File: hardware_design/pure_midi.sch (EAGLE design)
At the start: 60 parts, among them IC1 74HC165D, IC2 VOLTAGE_REG_POS05DT, Q1 20MHz, T1 MMBT3904, T2 MMBT3904, T3 MMBT3904, T4 MMBT3904, U1 ANALOG_DEVICES_INC_AD5754AREZ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, U2 TEXAS_INSTRUMENTS_LM4040C25ID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, U3 ATMEGA328P_TQFP, X1 OG-MIDI_MAB5SHCUI-SD-50BV

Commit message: Use different one-hot to binary encoder
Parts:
- removed IC1: 74HC165D, 74xx-eu:74HC165D
- added IC3: 74HC148D, 74xx-eu:74HC148D
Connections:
- removed net N$17: IC1A.B, R24.2, U$12.2
- removed net N$18: IC1A.C, R23.2, U$12.3
- removed net N$19: IC1A.D, R22.2, U$12.4
- removed net N$21: IC1A.E, R21.2, U$12.5
- removed net N$22: IC1A.F, R20.2, U$12.6
- removed net N$23: IC1A.G, R19.2, U$12.7
- removed net N$24: IC1A.H, R18.2, U$12.8
- removed net ROTARY_CLK: IC1A.CLK, U3.PD4(XCK/T0)
- removed net ROTARY_DAT: IC1A.QH, U3.PD2(INT0)
- removed net ROTARY_LD: IC1A.SH/!LD, U3.PD3(INT1)
- new net N$26: IC3A.1, R19.1, U$12.2
- new net N$27: IC3A.2, R20.1, U$12.3
- new net N$28: IC3A.3, R21.1, U$12.4
- new net N$29: IC3A.4, R22.1, U$12.5
- new net N$30: IC3A.5, R23.1, U$12.6
- new net N$31: IC3A.6, R24.1, U$12.7
- new net N$32: IC3A.7, R25.1, U$12.8
- new net ROTARY_D0: IC3A.A0, U3.PD2(INT0)
- new net ROTARY_D1: IC3A.A1, U3.PD3(INT1)
- new net ROTARY_D2: IC3A.A2, U3.PD4(XCK/T0)
- net +5V: now also IC3P.VCC, R18.2, R19.2, R20.2, R21.2, R22.2, R23.2, R24.2, R25.2; no longer IC1P.VCC, U$12.A
- net GND: now also IC3A.EI, IC3P.GND, U$12.A; no longer IC1A.INH, IC1P.GND, R18.1, R19.1, R20.1, R21.1, R22.1, R23.1, R24.1, R25.1
- net N$15: now also IC3A.0, R18.1; no longer IC1A.A, R25.2
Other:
- moved on the sheet: R18, R19, R20, R21, R22, R23, R24, R25, U$12

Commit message: Add USB Interface (completely untested)
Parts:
- added C10, C11, C12, C13, C14, C15, C16, C9: 100n, rcl:C-EUC0805
- added C6: 47u, GMSN:CAPACITOR_POL-US153CLV-0505
- added C7, C8: 22p, rcl:C-EUC0805
- added IC1, IC4: 74HCT125D, 74xx-eu:74HCT125D
- added IC1_33: VOLTAGE_REG_POSDT, GMSN:VOLTAGE_REG_POSDT
- added Q2: (no value), adafruit:CRYSTALHC49UP
- added R26, R27: 33R, rcl:R-EU_R0805
- added U4: MAX3421, SparkFun-IC-Comms:MAX3421ESMD
- added X2: KUSBVX, con-kycon:KUSBVX
- C3, C4, C5: value (none) -> 47u
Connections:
- net SS renamed SS_DAC
- new net +3V3: C14.1, C16.1, C6.+, IC1P.VCC, IC1_33.VO, U4.VCC, U4.VL
- new net INT_USB: IC4B.O, U3.PB1(OC1A)
- new net INT_USB_3V3: IC4B.I, U4.INT
- new net MISO_3V3: IC4A.I, U4.MISO
- new net MOSI_3V3: IC1C.O, U4.MOSI
- new net N$19: C8.2, Q2.2, U4.X0
- new net N$25: C7.2, Q2.1, U4.X1
- new net RES_USB_3V3: U4.RES
- new net RST_USB: IC1D.I, U3.PD7(AIN1)
- new net RST_USB_3V3: IC1D.O
- new net SCK_3V3: IC1A.O, U4.SCK
- new net SS_USB: IC1B.I, IC4A.OE, U3.PB0(ICP)
- new net SS_USB_3V3: IC1B.O, U4.SS
- new net USB_D_N: R26.1, X2.2
- new net USB_D_P: R27.1, X2.3
- new net USB_N: R26.2, U4.D-
- new net USB_P: R27.2, U4.D+
- new net USB_VBUS: X2.1
- net +12V: now also C11.1, IC1_33.VI
- net +5V: now also C12.1, C13.1, C15.1, C9.1, IC4P.VCC
- net -12V: now also C10.2
- net GND: now also C10.1, C11.2, C12.2, C13.2, C14.2, C15.2, C16.2, C6.-, C7.1, C8.1, C9.2, IC1A.OE, IC1B.OE, IC1C.OE, IC1D.OE, IC1P.GND, IC1_33.GND, IC4B.OE, IC4P.GND, U4.GND@19, U4.GND@3, X2.4, X2.S1, X2.S2
- net MISO: now also IC4A.O
- net MOSI: now also IC1C.I
- net SCK: now also IC1A.I

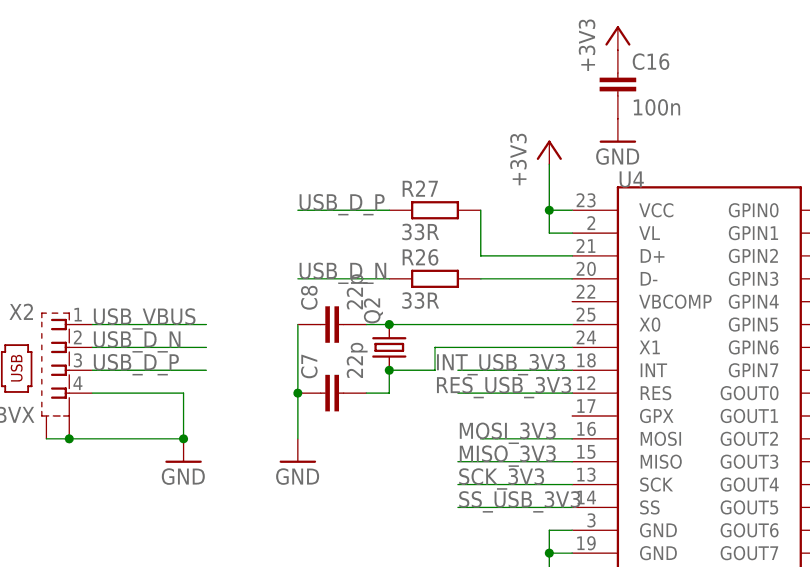
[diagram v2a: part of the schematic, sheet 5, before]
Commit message: Specify USB Host Clock Frequency
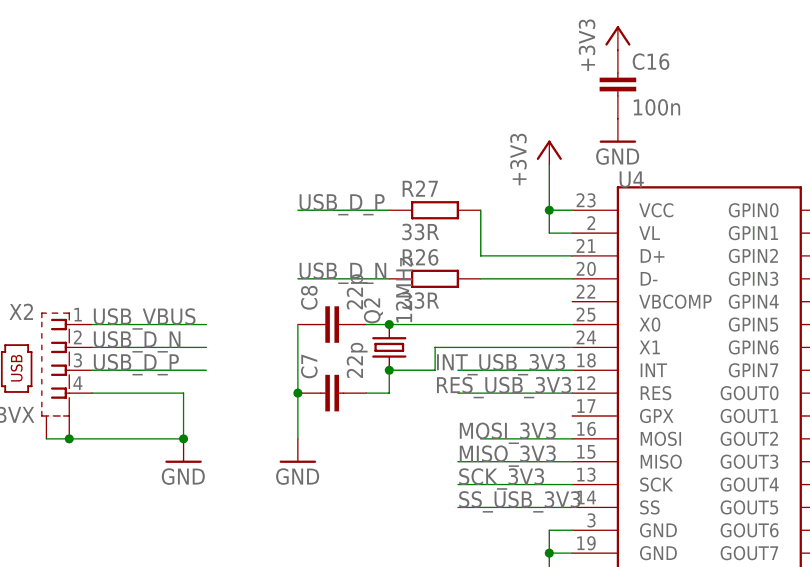
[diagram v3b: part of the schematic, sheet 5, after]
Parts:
- Q2: value (none) -> 12MHz
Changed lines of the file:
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@@
 <part name="C6" library="GMSN" deviceset="CAPACITOR_POL-US" device="153CLV-0505" value="47u"/>
 <part name="+3V1" library="supply1" library_urn="urn:adsk.eagle:library:371" deviceset="+3V3" device=""/>
-<part name="Q2" library="adafruit" library_urn="urn:adsk.eagle:library:420" deviceset="CRYSTAL" device="HC49UP" package3d_urn="urn:adsk.eagle:package:6240908/1"/>
+<part name="Q2" library="adafruit" library_urn="urn:adsk.eagle:library:420" deviceset="CRYSTAL" device="HC49UP" package3d_urn="urn:adsk.eagle:package:6240908/1" value="12MHz"/>
 <part name="C7" library="rcl" library_urn="urn:adsk.eagle:library:334" deviceset="C-EU" device="C0805" package3d_urn="urn:adsk.eagle:package:23617/2" value="22p"/>
 <part name="C8" library="rcl" library_urn="urn:adsk.eagle:library:334" deviceset="C-EU" device="C0805" package3d_urn="urn:adsk.eagle:package:23617/2" value="22p"/>

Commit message: First Revision
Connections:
- removed net AGND: T1.E, T2.E, T3.E, T4.E, U$1.1, U$2.1, U$3.1, U$4.1, U$5.1, U$6.1, U$7.1, U$8.1, U1.1_DAC_GND, U1.1_SIG_GND, U1.2_DAC_GND, U1.2_SIG_GND, U2.ANODE, U3.AGND
- removed net RES_USB_3V3: U4.RES
- removed net USB_VBUS: X2.1
- net +5V: now also X2.1
- net GND: now also T1.E, T2.E, T3.E, T4.E, U$1.1, U$2.1, U$3.1, U$4.1, U$5.1, U$6.1, U$7.1, U$8.1, U1.1_DAC_GND, U1.1_SIG_GND, U1.2_DAC_GND, U1.2_SIG_GND, U2.ANODE, U3.AGND
- net RST_USB_3V3: now also U4.RES
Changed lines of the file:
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@@
 <class number="0" name="default" width="0" drill="0">
+</class>
+<class number="1" name="POWER" width="0.3556" drill="0">
 </class>
 </classes>
@@
 <part name="+3V4" library="supply1" library_urn="urn:adsk.eagle:library:371" deviceset="+3V3" device=""/>
 <part name="GND30" library="supply1" library_urn="urn:adsk.eagle:library:371" deviceset="GND" device=""/>
+<part name="P+23" library="supply1" library_urn="urn:adsk.eagle:library:371" deviceset="+5V" device=""/>
 </parts>
 <sheets>
@@
 </segment>
 </net>
-<net name="GND" class="0">
+<net name="GND" class="1">
 <segment>
 <pinref part="ISP1" gate="G$1" pin="GND"/>
@@
 <pinref part="GND26" gate="1" pin="GND"/>
 </segment>
-</net>
-<net name="+5V" class="0">
+<segment>
+<pinref part="U3" gate="U$1" pin="AGND"/>
+<pinref part="AGND15" gate="VR1" pin="AGND"/>
+<wire x1="40.64" y1="30.48" x2="33.02" y2="30.48" width="0.1524" layer="91"/>
+</segment>
+</net>
+<net name="+5V" class="1">
 <segment>
 <pinref part="ISP1" gate="G$1" pin="VCC"/>
@@
 </segment>
 </net>
-<net name="AGND" class="0">
-<segment>
-<pinref part="U3" gate="U$1" pin="AGND"/>
-<pinref part="AGND15" gate="VR1" pin="AGND"/>
-<wire x1="40.64" y1="30.48" x2="33.02" y2="30.48" width="0.1524" layer="91"/>
-</segment>
-</net>
 <net name="SWITCH0_VAL" class="0">
 <segment>
@@
 </busses>
 <nets>
-<net name="AGND" class="0">
+<net name="GND" class="1">
+<segment>
+<pinref part="U1" gate="G$0" pin="GND"/>
+<pinref part="GND1" gate="1" pin="GND"/>
+<wire x1="114.3" y1="20.32" x2="121.92" y2="20.32" width="0.1524" layer="91"/>
+<wire x1="121.92" y1="20.32" x2="121.92" y2="17.78" width="0.1524" layer="91"/>
+</segment>
+<segment>
+<pinref part="GND2" gate="1" pin="GND"/>
+<pinref part="U1" gate="G$0" pin="BIN/!2SCOMP!"/>
+<wire x1="58.42" y1="45.72" x2="73.66" y2="45.72" width="0.1524" layer="91"/>
+<pinref part="U1" gate="G$0" pin="!LDAC!"/>
+<wire x1="73.66" y1="50.8" x2="58.42" y2="50.8" width="0.1524" layer="91"/>
+<wire x1="58.42" y1="50.8" x2="58.42" y2="45.72" width="0.1524" layer="91"/>
+<junction x="58.42" y="45.72"/>
+</segment>
+<segment>
+<pinref part="C11" gate="G$1" pin="2"/>
+<pinref part="GND27" gate="1" pin="GND"/>
+</segment>
+<segment>
+<pinref part="C12" gate="G$1" pin="2"/>
+<pinref part="GND28" gate="1" pin="GND"/>
+</segment>
+<segment>
+<pinref part="C10" gate="G$1" pin="1"/>
+<wire x1="106.68" y1="93.98" x2="106.68" y2="96.52" width="0.1524" layer="91"/>
+<pinref part="GND29" gate="1" pin="GND"/>
+<wire x1="106.68" y1="96.52" x2="116.84" y2="96.52" width="0.1524" layer="91"/>
+</segment>
 <segment>
 <pinref part="AGND1" gate="VR1" pin="AGND"/>
@@
 </segment>
 </net>
-<net name="GND" class="0">
-<segment>
-<pinref part="U1" gate="G$0" pin="GND"/>
-<pinref part="GND1" gate="1" pin="GND"/>
-<wire x1="114.3" y1="20.32" x2="121.92" y2="20.32" width="0.1524" layer="91"/>
-<wire x1="121.92" y1="20.32" x2="121.92" y2="17.78" width="0.1524" layer="91"/>
-</segment>
-<segment>
-<pinref part="GND2" gate="1" pin="GND"/>
-<pinref part="U1" gate="G$0" pin="BIN/!2SCOMP!"/>
-<wire x1="58.42" y1="45.72" x2="73.66" y2="45.72" width="0.1524" layer="91"/>
-<pinref part="U1" gate="G$0" pin="!LDAC!"/>
-<wire x1="73.66" y1="50.8" x2="58.42" y2="50.8" width="0.1524" layer="91"/>
-<wire x1="58.42" y1="50.8" x2="58.42" y2="45.72" width="0.1524" layer="91"/>
-<junction x="58.42" y="45.72"/>
-</segment>
-<segment>
-<pinref part="C11" gate="G$1" pin="2"/>
-<pinref part="GND27" gate="1" pin="GND"/>
-</segment>
-<segment>
-<pinref part="C12" gate="G$1" pin="2"/>
-<pinref part="GND28" gate="1" pin="GND"/>
-</segment>
-<segment>
-<pinref part="C10" gate="G$1" pin="1"/>
-<wire x1="106.68" y1="93.98" x2="106.68" y2="96.52" width="0.1524" layer="91"/>
-<pinref part="GND29" gate="1" pin="GND"/>
-<wire x1="106.68" y1="96.52" x2="116.84" y2="96.52" width="0.1524" layer="91"/>
-</segment>
-</net>
-<net name="-12V" class="0">
+<net name="-12V" class="1">
 <segment>
 <pinref part="P-1" gate="1" pin="-12V"/>
@@
 </segment>
 </net>
-<net name="+12V" class="0">
+<net name="+12V" class="1">
 <segment>
 <pinref part="U1" gate="G$0" pin="AVDD"/>
@@
 </segment>
 </net>
-<net name="+5V" class="0">
+<net name="+5V" class="1">
 <segment>
 <pinref part="U1" gate="G$0" pin="DVCC"/>
@@
 </segment>
 </net>
-<net name="+5V" class="0">
+<net name="+5V" class="1">
 <segment>
 <wire x1="68.58" y1="50.8" x2="71.12" y2="50.8" width="0.1524" layer="91"/>
@@
 </segment>
 </net>
-<net name="GND" class="0">
+<net name="GND" class="1">
 <segment>
 <pinref part="GND6" gate="1" pin="GND"/>
@@
 </busses>
 <nets>
-<net name="GND" class="0">
+<net name="GND" class="1">
 <segment>
 <pinref part="U$12" gate="G$1" pin="A"/>
@@
 </segment>
 </net>
-<net name="+5V" class="0">
+<net name="+5V" class="1">
 <segment>
 <pinref part="R18" gate="G$1" pin="2"/>
@@
 <attribute name="VALUE" x="88.9" y="55.88" size="1.778" layer="96"/>
 </instance>
+<instance part="P+23" gate="1" x="45.72" y="45.72" smashed="yes">
+<attribute name="VALUE" x="43.18" y="40.64" size="1.778" layer="96" rot="R90"/>
+</instance>
 </instances>
 <busses>
 </busses>
 <nets>
-<net name="GND" class="0">
+<net name="GND" class="1">
 <segment>
 <pinref part="X2" gate="G$1" pin="4"/>
@@
 </segment>
 </net>
-<net name="USB_VBUS" class="0">
-<segment>
-<pinref part="X2" gate="G$1" pin="1"/>
-<wire x1="33.02" y1="38.1" x2="45.72" y2="38.1" width="0.1524" layer="91"/>
-<label x="33.02" y="38.1" size="1.778" layer="95"/>
-</segment>
-</net>
 <net name="USB_P" class="0">
 <segment>
@@
 <pinref part="IC1" gate="B" pin="O"/>
 <wire x1="88.9" y1="81.28" x2="96.52" y2="81.28" width="0.1524" layer="91"/>
+<label x="88.9" y="81.28" size="1.778" layer="95"/>
 </segment>
 </net>
@@
 <label x="127" y="78.74" size="1.778" layer="95"/>
 </segment>
+<segment>
+<pinref part="U4" gate="G$1" pin="RES"/>
+<wire x1="86.36" y1="30.48" x2="73.66" y2="30.48" width="0.1524" layer="91"/>
+<label x="71.12" y="30.48" size="1.778" layer="95"/>
+</segment>
 </net>
 <net name="MISO" class="0">
@@
 </segment>
 </net>
-<net name="RES_USB_3V3" class="0">
-<segment>
-<pinref part="U4" gate="G$1" pin="RES"/>
-<wire x1="86.36" y1="30.48" x2="73.66" y2="30.48" width="0.1524" layer="91"/>
-<label x="71.12" y="30.48" size="1.778" layer="95"/>
-</segment>
-</net>
-<net name="+5V" class="0">
+<net name="+5V" class="1">
 <segment>
 <pinref part="IC4" gate="P" pin="VCC"/>
@@
 <wire x1="218.44" y1="114.3" x2="210.82" y2="114.3" width="0.1524" layer="91"/>
 <junction x="210.82" y="114.3"/>
+</segment>
+<segment>
+<pinref part="X2" gate="G$1" pin="1"/>
+<wire x1="33.02" y1="38.1" x2="45.72" y2="38.1" width="0.1524" layer="91"/>
+<label x="33.02" y="38.1" size="1.778" layer="95"/>
+<pinref part="P+23" gate="1" pin="+5V"/>
+<wire x1="45.72" y1="43.18" x2="45.72" y2="38.1" width="0.1524" layer="91"/>
 </segment>
 </net>
@@
 </segment>
 </net>
-<net name="+5V" class="0">
+<net name="+5V" class="1">
 <segment>
 <pinref part="IC2" gate="A1" pin="VO"/>
@@
 </segment>
 </net>
-<net name="-12V" class="0">
+<net name="-12V" class="1">
 <segment>
 <pinref part="C4" gate="G$1" pin="-"/>
@@
 </segment>
 </net>
-<net name="+12V" class="0">
+<net name="+12V" class="1">
 <segment>
 <pinref part="D2" gate="G$1" pin="C"/>
@@
 </segment>
 </net>
-<net name="GND" class="0">
+<net name="GND" class="1">
 <segment>
 <pinref part="PWR1" gate="G$1" pin="7"/>

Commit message: Rev 1/2
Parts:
- removed IC1_33: VOLTAGE_REG_POSDT, GMSN:VOLTAGE_REG_POSDT
- removed ISP1: AVRISP-6, adafruit:AVRISP-6
- removed JP1: (no value), jumper:JP1E
- removed OK1: 6N138, optocoupler:6N138
- removed Q1: 20MHz, adafruit:CRYSTALHC49UP
- removed Q2: 12MHz, adafruit:CRYSTALHC49UP
- removed R22, R23, R24, R25: 10k, rcl:R-EU_R0805
- removed T1, T2, T3, T4: MMBT3904, transistor:-NPN-SOT23-EBC
- removed U$10, U$9: TOGGLE_ON_OFF_ON, INSTRUO:TOGGLE_ON_OFF_ON
- added C17, C21, C23, C24, C25, C26: 100n, rcl:C-EUC0603
- added DI1: OLED_1.3_128X64_SPI, microbuilder:OLED_1.3_128X64_SPI
- added FD1, FD2, FD3, FD4: FIDUCIALUFIDUCIAL, SparkFun-Aesthetics:FIDUCIALUFIDUCIAL
- added IC5: STM32F10XCXT6, stm32:STM32F10XCXT6
- added IC6: LD117AS33TR, v-reg:LD117AS33TR
- added J1: CORTEX_DEBUG_PTH, SparkFun-Connectors:CORTEX_DEBUG_PTH
- added LOGO1: OSHW-LOGOM, SparkFun-Aesthetics:OSHW-LOGOM
- added SW1: EC12E_SW, switch-alps:EC12E_SW
- added U$13, U$14, U$15, U$16, U$17, U$18, U$19, U$20: WQP-PJ301M-12_JACK, thonkiconn:WQP-PJ301M-12_JACK
- added U5: TEXAS_INSTRUMENTS_LM4040C25IDBZRTEXAS_INSTRUMENTS_LM4040C25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, lm4040:TEXAS_INSTRUMENTS_LM4040C25IDBZRTEXAS_INSTRUMENTS_LM4040C25IDBZR_0_1
- added X3: OG-MIDI_MAB5SHCUI-SD-50BV, yarns_v03:OG-MIDI_MAB5SHCUI-SD-50BV
- added X4: KUSBVX-BS1N, con-kycon:KUSBVX-BS1N
- added X6: ABRACON_ABM3B-12.000MHZ-B2-TABRACON_ABM3B-12.000MHZ-B2-T_0_0, Abracon - ABM3B-12.000MHZ-B2-T:ABRACON_ABM3B-12.000MHZ-B2-TABRACON_ABM3B-12.000MHZ-B2-T_0_0
- added X7: ABRACON_ABM3B-8.000MHZ-B2-TABRACON_ABM3B-8.000MHZ-B2-T_0_0, Abracon - ABM3B-8.000MHZ-B2-T:ABRACON_ABM3B-8.000MHZ-B2-TABRACON_ABM3B-8.000MHZ-B2-T_0_0
- C1, C10, C11, C12, C13, C14, C15, C16, C2, C7, C8, C9: device rcl:C-EUC0805 -> rcl:C-EUC0603
- C3, C4, C5, C6: value 47u -> 22u
- IC1: value 74HCT125D -> LD117AS50TR; device 74xx-eu:74HCT125D -> v-reg:LD117AS50TR
- IC2: value VOLTAGE_REG_POS05DT -> 74HCT125D; device GMSN:VOLTAGE_REG_POS05DT -> 74xx-eu:74HCT125D
- IC3: value 74HC148D -> 6N138SMD; device 74xx-eu:74HC148D -> 6n138:6N138SMD
- R1: value 2k -> 1k; device rcl:R-EU_R0805 -> rcl:R-EU_R0603
- R10, R9: value 1k -> 51R; device rcl:R-EU_R0805 -> rcl:R-EU_R0603
- R11, R12, R17: device resistor:R-EU_R0805 -> rcl:R-EU_R0603
- R13, R14: value 10k -> 22R; device resistor:R-EU_R0805 -> rcl:R-EU_R0603
- R15, R16: device resistor:R-EU_R0805 -> resistor:R-EU_R0603
- R18, R19: value 10k -> 2k; device rcl:R-EU_R0805 -> rcl:R-EU_R0603
- R2, R21, R26, R27, R4, R5, R6, R7, R8: device rcl:R-EU_R0805 -> rcl:R-EU_R0603
- R20: value 10k -> 1k5; device rcl:R-EU_R0805 -> rcl:R-EU_R0603
- R3: value 1k -> 4k7; device rcl:R-EU_R0805 -> rcl:R-EU_R0603
- U$11: value Q-POT -> WQP-PJ301M-12_JACK; device INSTRUO:Q-POT -> thonkiconn:WQP-PJ301M-12_JACK
- U$12: value ALPS-SRBV -> WQP-PJ301M-12_JACK; device TomW:ALPS-SRBV -> thonkiconn:WQP-PJ301M-12_JACK
- U1: value ANALOG_DEVICES_INC_AD5754AREZANALOG_DEVICES_INC_AD5754AREZ_0_0 -> AD5676ARUZ; device Analog Devices Inc - AD5754AREZ:ANALOG_DEVICES_INC_AD5754AREZANALOG_DEVICES_INC_AD5754AREZ_0_0 -> AD5676ARUZ:AD5676ARUZ
- U2: value TEXAS_INSTRUMENTS_LM4040C25IDBZRTEXAS_INSTRUMENTS_LM4040C25IDBZR_0_1 -> AD5754BREZ; device Texas Instruments - LM4040C25IDBZR:TEXAS_INSTRUMENTS_LM4040C25IDBZRTEXAS_INSTRUMENTS_LM4040C25IDBZR_0_1 -> ad5754:AD5754BREZ
- U3: value ATMEGA328P_TQFP -> TEXAS_INSTRUMENTS_LM4040C5IDBZR1; device SparkFun-IC-Microcontroller:ATMEGA328P_TQFP -> lm4040:TEXAS_INSTRUMENTS_LM4040C5IDBZR1
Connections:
- removed net AREF: R1.1, U1.REFIN, U2.CATHODE
- removed net INT_USB_3V3: IC4B.I, U4.INT
- removed net MISO_3V3: IC4A.I, U4.MISO
- removed net MOSI_3V3: IC1C.O, U4.MOSI
- removed net N$16: R14.2, U$9.O
- removed net N$25: C7.2, Q2.1, U4.X1
- removed net N$26: IC3A.1, R19.1, U$12.2
- removed net N$27: IC3A.2, R20.1, U$12.3
- removed net N$28: IC3A.3, R21.1, U$12.4
- removed net N$29: IC3A.4, R22.1, U$12.5
- removed net N$30: IC3A.5, R23.1, U$12.6
- removed net N$31: IC3A.6, R24.1, U$12.7
- removed net N$32: IC3A.7, R25.1, U$12.8
- removed net ROTARY_D0: IC3A.A0, U3.PD2(INT0)
- removed net ROTARY_D1: IC3A.A1, U3.PD3(INT1)
- removed net ROTARY_D2: IC3A.A2, U3.PD4(XCK/T0)
- removed net RST_USB_3V3: IC1D.O, U4.RES
- removed net SCK_3V3: IC1A.O, U4.SCK
- removed net SPEED_VAL: U$11.2, U3.PC4(ADC4/SDA)
- removed net SS_DAC: U1.!SYNC!, U3.PB2(SS/OC1B)
- removed net SS_USB_3V3: IC1B.O, U4.SS
- removed net SWITCH0_VAL: R13.1, U$9.P, U3.ADC6
- removed net SWITCH1_VAL: R15.1, U$10.P, U3.ADC7
- new net AREF_25: R18.1, U2.REFIN, U5.CATHODE
- new net AREF_5: R19.1, U1.VREF, U3.CATHODE
- new net CV_OUT_10: U$16.2, U1.VOUT5
- new net CV_OUT_11: U$17.2, U1.VOUT6
- new net CV_OUT_12: U$18.2, U1.VOUT7
- new net CV_OUT_5: U$11.2, U1.VOUT0
- new net CV_OUT_6: U$12.2, U1.VOUT1
- new net CV_OUT_7: U$13.2, U1.VOUT2
- new net CV_OUT_8: U$14.2, U1.VOUT3
- new net CV_OUT_9: U$15.2, U1.VOUT4
- new net D_GATE_OUT_5: IC4C.I, IC5PORTA_L.PA4
- new net D_GATE_OUT_6: IC4D.I, IC5PORTA_L.PA5
- new net ENC_A: IC5PORTC.PC13, R15.1, SW1G$1.A
- new net ENC_B: IC5PORTC.PC14, R16.1, SW1G$1.B
- new net ENC_SW: IC5PORTC.PC15, SW1G$2.2
- new net GATE_OUT_5: R7.1, U$19.2
- new net GATE_OUT_6: R8.1, U$20.2
- new net JTCK: IC5PORTA_H.PA14, J1.SWDCLK/TCK
- new net JTDI: IC5PORTA_H.PA15, J1.NC/TDI
- new net JTDO: IC5PORTB_L.PB3, J1.SWO/TDO
- new net JTMS: IC5PORTA_H.PA13, J1.SWDIO/TMS
- new net MIDI_DATA_OUT: IC5PORTA_H.PA9, R9.1
- new net N$17: IC4C.O, R7.2
- new net N$18: IC4D.O, R8.2
- new net N$21: R13.1, X4.2
- new net N$22: R10.1, X3.4
- new net N$23: R14.1, R20.2, X4.3
- new net SDC_OLED: DI1.SDC, IC5PORTB_H.PB12
- new net SS_DAC0: IC5PORTB_L.PB6, U1.!SYNC
- new net SS_DAC1: IC5PORTB_L.PB7, U2.SYNC
- new net SS_OLED: DI1.CCS, IC5PORTB_H.PB11
- new net USB_PER_D_N: IC5PORTA_H.PA11, R13.2
- new net USB_PER_D_P: IC5PORTA_H.PA12, R14.2
- net +12V: now also C13.1, IC1.IN, IC6.IN, R18.2, R19.2, U1.VDD, U2.AVDD; no longer IC1_33.VI, IC2.VI, R1.2, R10.1, R5.1, R7.1, R8.1, U1.AVDD
- net +3V3: now also C15.1, C21.1, C23.1, C24.1, C25.1, IC3.VCC, IC5AN_POWER.VBAT, IC5AN_POWER.VDDA, IC5POWER.VDD_1, IC5POWER.VDD_2, IC5POWER.VDD_3, IC6.OUT, J1.VCC, R10.2, R12.2, R20.1, R21.2; no longer IC1P.VCC, IC1_33.VO
- net +5V: now also C10.1, C17.1, DI1.VCC, IC1.OUT, IC2P.VCC, R16.2, R3.2, U1.VLOGIC, U2.DVCC; no longer C13.1, C15.1, IC2.VO, IC3P.VCC, ISP1.VCC, OK1.VCC, R12.2, R13.2, R18.2, R19.2, R20.2, R21.2, R22.2, R23.2, R24.2, R25.2, U$11.3, U1.DVCC, U3.AVCC, U3.VCC@4, U3.VCC@6
- net -12V: now also C26.2, U2.AVSS, U2.AVSS_2; no longer C10.2, U1.AVSS, U1.EP
- net CV_OUT_1: now also U2.VOUTA; no longer U1.VOUTA
- net CV_OUT_2: now also U2.VOUTB; no longer U1.VOUTB
- net CV_OUT_3: now also U2.VOUTC; no longer U1.VOUTC
- net CV_OUT_4: now also U2.VOUTD; no longer U1.VOUTD
- net D_GATE_OUT_1: now also IC2A.I, IC5PORTA_L.PA0; no longer R3.2, U3.PC5(ADC5/SCL)
- net D_GATE_OUT_2: now also IC2B.I, IC5PORTA_L.PA1; no longer R6.2, U3.PC1(ADC1)
- net D_GATE_OUT_3: now also IC2C.I, IC5PORTA_L.PA2; no longer R4.2, U3.PC2(ADC2)
- net D_GATE_OUT_4: now also IC2D.I, IC5PORTA_L.PA3; no longer R9.2, U3.PC3(ADC3)
- net GATE_OUT_1: now also R1.1; no longer R7.2, T1.C
- net GATE_OUT_2: now also R4.1; no longer R8.2, T3.C
- net GATE_OUT_3: now also R5.1; no longer R5.2, T2.C
- net GATE_OUT_4: now also R6.1; no longer R10.2, T4.C
- net GND: now also C10.2, C17.2, C21.2, C23.2, C24.2, C25.2, C26.1, DI1.GND, IC1.ADJ, IC2A.OE, IC2B.OE, IC2C.OE, IC2D.OE, IC2P.GND, IC3.GND, IC4C.OE, IC4D.OE, IC5AN_POWER.VSSA, IC5PORTB_L.PB2, IC5POWER.VSS_1, IC5POWER.VSS_2, IC5POWER.VSS_3, IC5RESET.BOOT0, IC6.ADJ, J1.GND@3, J1.GND@5, J1.GNDDTCT, SW1G$1.C, SW1G$2.1, U$12.1, U$13.1, U$14.1, U$15.1, U$16.1, U$17.1, U$18.1, U$19.1, U$20.1, U1.!LDAC, U1.RSTSEL, U2.BIN/_2SCOMP, U2.DAC_GND, U2.DAC_GND_2, U2.GND, U2.LDAC, U2.SIG_GND, U2.SIG_GND_2, U3.ANODE, U5.ANODE, X3.2, X4.4, X4.S1, X4.S2, X6.1_GND, X6.2_GND, X7.1_GND, X7.2_GND; no longer C10.1, IC1A.OE, IC1B.OE, IC1C.OE, IC1D.OE, IC1P.GND, IC1_33.GND, IC2.GND, IC3A.EI, IC3P.GND, IC4B.OE, ISP1.GND, OK1.GND, R14.1, R16.1, T1.E, T2.E, T3.E, T4.E, U$10.S, U$12.A, U$9.S, U1.!LDAC!, U1.1_DAC_GND, U1.1_SIG_GND, U1.2_DAC_GND, U1.2_SIG_GND, U1.BIN/!2SCOMP!, U2.ANODE, U3.AGND, U3.GND@3, U3.GND@5
- net INT_USB: now also IC5PORTB_H.PB10, U4.INT; no longer IC4B.O, U3.PB1(OC1A)
- net MIDI_DATA_IN: now also IC3.VO, IC5PORTA_H.PA10; no longer JP1.2, OK1.VO
- net MISO: now also IC5PORTB_H.PB14, U4.MISO; no longer IC4A.O, ISP1.MISO, U3.PB4(MISO)
- net MOSI: now also DI1.MOSI, IC5PORTB_H.PB15, U1.SDI, U2.SDIN, U4.MOSI; no longer IC1C.I, ISP1.MOSI, U1.SDIN, U3.PB3(MOSI/OC2)
- net N$1: now also U1.GAIN; no longer U1.!CLR!
- net N$10: now also IC2A.O, R1.2; no longer JP1.1, U3.PD0(RXD)
- net N$11: now also IC2B.O, R4.2; no longer R9.1, T4.B
- net N$12: now also IC3.VB; no longer OK1.VB
- net N$14: now also IC2C.O, R5.2; no longer R16.2, U$10.O
- net N$15: now also IC2D.O, R6.2; no longer IC3A.0, R18.1, U$12.1
- net N$19: now also R9.2, X3.5; no longer C8.2, Q2.2, U4.X0
- net N$2: now also U2.CLR; no longer T1.B
- net N$3: now also C2.2, IC5PORTD/OSC.PD1/OSC=>, X7.X2; no longer R4.1, T2.B
- net N$4: now also IC3.A; no longer OK1.A
- net N$6: now also IC5PORTD/OSC.PD0/OSC<=, X7.X1; no longer Q1.2, U3.PB6(XTAL1/TOSC1)
- net N$7: now also C8.2, U4.X0, X6.X1; no longer C2.2, Q1.1, U3.PB7(XTAL2/TOSC2)
- net N$8: now also C7.2, U4.X1, X6.X2; no longer R6.1, T3.B
- net N$9: now also IC3.C; no longer OK1.C
- net RST: now also DI1.RES, IC5RESET.NRST, J1.!RESET, R21.1, U1.!RESET; no longer ISP1.RST, U3.PC6(/RESET)
- net RST_USB: now also IC5PORTB_H.PB8, U4.RES; no longer IC1D.I, U3.PD7(AIN1)
- net SCK: now also DI1.CLK, IC5PORTB_H.PB13, U2.SCLK, U4.SCK; no longer IC1A.I, ISP1.SCK, U3.PB5(SCK)
- net SS_USB: now also IC5PORTB_H.PB9, U4.SS; no longer IC1B.I, IC4A.OE, U3.PB0(ICP)
